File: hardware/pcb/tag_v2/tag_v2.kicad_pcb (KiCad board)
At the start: 2 copper layers, 87.6 x 50.8 mm, 16 parts

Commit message: *: Update after the first PCB assembly.
- Replaced the 200k ohm resistor with 100k ohm on tag_v2, as GPIO pin 32
  reduces the voltage somehow, updated the battery voltage divider
  accordingly in tag.ino

- Fix an issue of tag LED as the tag will not invoke newDevice() even
  though it's added by the Sensor.

- Updated the DRIVE_MODE_MANUAL to be long steady light instead of
  blincking.

- Fixed a short wiring issue on the sensor.
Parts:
- R5: value 220KΩ -> 100KΩ
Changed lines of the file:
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@@
 			)
 		)
-		(property "Value" "220KΩ"
+		(property "Value" "100KΩ"
 			(at 3.81 0 90)
 			(unlocked yes)

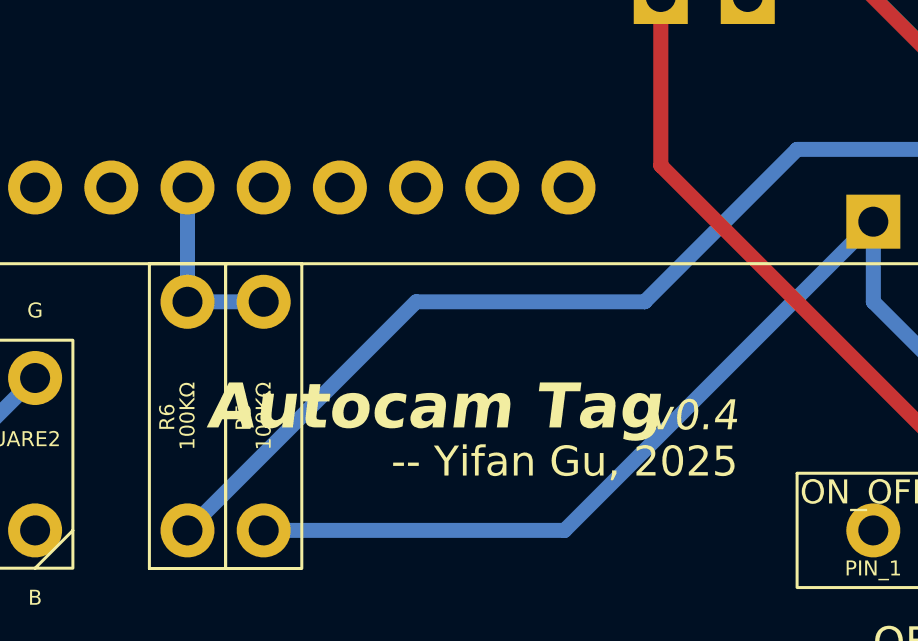
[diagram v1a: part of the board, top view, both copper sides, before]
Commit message: remote: Update PCB for remote.
Fix the issue that GPIO 35 does not have internal PULLUP resistor.
So switch the pin with the gimbal thumbstick input Y, instead of the
drive mode button.

Update sensor and tag pcb as well to reflect the changes.
- tag: Use pin 39 for battery measurement and revert the resistor value
  change that's done in the previous commit.
- sensor: Fix a wiring issue.
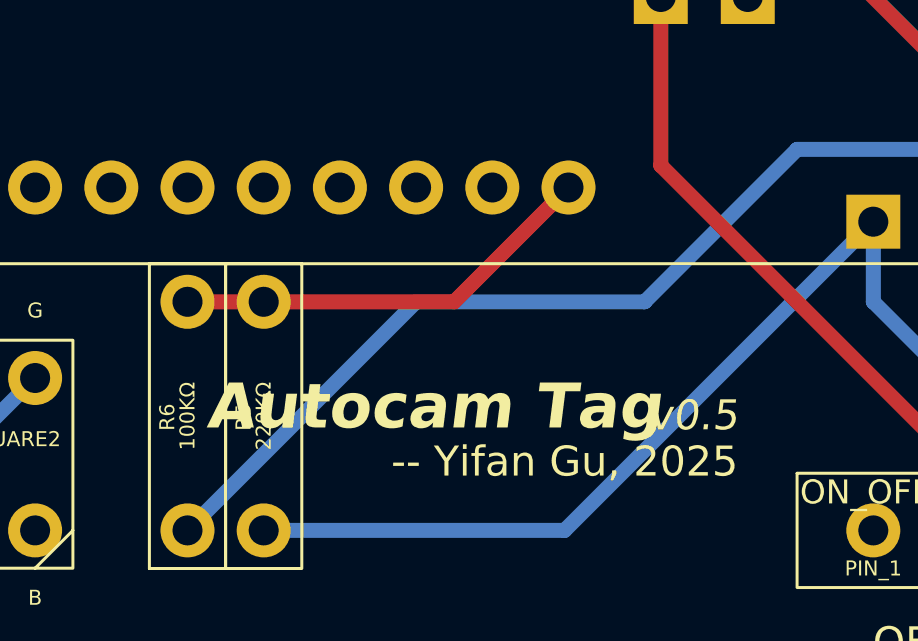
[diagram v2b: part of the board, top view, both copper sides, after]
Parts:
- R5: value 100KΩ -> 220KΩ
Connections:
- ESP32_UWB1 pad 15: Net-(ESP32_UWB1-IO32) -> unconnected-(ESP32_UWB1-IO32-Pad15)
- ESP32_UWB1 pad 20: unconnected-(ESP32_UWB1-IO39-Pad20) -> Net-(ESP32_UWB1-IO39)
- R5 pad 2: Net-(ESP32_UWB1-IO32) -> Net-(ESP32_UWB1-IO39)
- R6 pad 2: Net-(ESP32_UWB1-IO32) -> Net-(ESP32_UWB1-IO39)
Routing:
- net Net-(ESP32_UWB1-IO39): track 0.00 -> 14.3 mm
- net Net-(ESP32_UWB1-IO32): track 6.35 -> 0.00 mm
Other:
- board text added: "v0.5"
- board text removed: "v0.4"
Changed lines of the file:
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@@
 	(title_block
 		(title "Autocam Tag")
-		(date "2025-03-18")
-		(rev "v0.4")
+		(date "2025-03-27")
+		(rev "v0.5")
 	)
 	(layers
@@
 	(net 36 "Net-(ESP32_UWB1-IO2)")
 	(net 37 "unconnected-(ESP32_UWB1-IO15-Pad9)")
-	(net 38 "unconnected-(ESP32_UWB1-IO39-Pad20)")
-	(net 39 "Net-(ESP32_UWB1-IO32)")
+	(net 38 "Net-(ESP32_UWB1-IO39)")
+	(net 39 "unconnected-(ESP32_UWB1-IO32-Pad15)")
 	(net 40 "Net-(RGB_LED_SQUARE1-R)")
 	(net 41 "Net-(RGB_LED_SQUARE1-G)")
@@
 			(layers "*.Cu" "*.Mask")
 			(remove_unused_layers no)
-			(net 39 "Net-(ESP32_UWB1-IO32)")
+			(net 39 "unconnected-(ESP32_UWB1-IO32-Pad15)")
 			(pinfunction "IO32")
 			(pintype "bidirectional")
@@
 			(layers "*.Cu" "*.Mask")
 			(remove_unused_layers no)
-			(net 38 "unconnected-(ESP32_UWB1-IO39-Pad20)")
+			(net 38 "Net-(ESP32_UWB1-IO39)")
 			(pinfunction "IO39")
 			(pintype "bidirectional")
@@
 			(layers "*.Cu" "*.Mask")
 			(remove_unused_layers no)
-			(net 39 "Net-(ESP32_UWB1-IO32)")
+			(net 38 "Net-(ESP32_UWB1-IO39)")
 			(pintype "passive")
 		)
@@
 			)
 		)
-		(property "Value" "100KΩ"
+		(property "Value" "220KΩ"
 			(at 3.81 0 90)
 			(unlocked yes)
@@
 			(layers "*.Cu" "*.Mask")
 			(remove_unused_layers no)
-			(net 39 "Net-(ESP32_UWB1-IO32)")
+			(net 38 "Net-(ESP32_UWB1-IO39)")
 			(pintype "passive")
 		)
@@
 		(layer "Edge.Cuts")
 	)
-	(gr_text "v0.4"
+	(gr_text "v0.5"
 		(at 169.485555 119.942652 0)
 		(layer "F.SilkS")
@@
 			(justify right bottom)
 		)
-		(render_cache "v0.4" 0
+		(render_cache "v0.5" 0
 			(polygon
 				(pts
@@
 			(polygon
 				(pts
-					(xy 168.919339 119.273724) (xy 168.952434 118.896308) (xy 169.039018 118.994921) (xy 169.017341 119.249483)
-					(xy 168.952434 119.309384)
+					(xy 169.469191 118.881654) (xy 169.367341 118.975443) (xy 169.058069 118.975443) (xy 168.971546 118.881654)
 				)
 			)
 			(polygon
 				(pts
-					(xy 169.443728 119.381924) (xy 169.410634 119.757997) (xy 169.325332 119.659323) (xy 169.347008 119.404822)
-					(xy 169.411916 119.345043)
+					(xy 169.391522 119.772652) (xy 168.893877 119.772652) (xy 168.996947 119.678862) (xy 169.30622 119.678862)
+				)
+			)
+			(polygon
+				(pts
+					(xy 168.919339 119.273724) (xy 168.952434 118.899544) (xy 169.039018 118.994982) (xy 169.017341 119.249483)
+					(xy 168.952434 119.309384)
 				)
 			)
 			(polygon
 				(pts
-					(xy 169.360991 119.249483) (xy 169.382607 118.995104) (xy 169.485738 118.896308) (xy 169.452643 119.273724)
-					(xy 169.415702 119.309384)
+					(xy 169.443728 119.381924) (xy 169.410634 119.753112) (xy 169.325332 119.659262) (xy 169.347008 119.404883)
+					(xy 169.411916 119.345043)
 				)
 			)
@@
 	(segment
 		(start 153.67 115.57)
-		(end 151.13 115.57)
+		(end 160.02 115.57)
 		(width 0.5)
-		(layer "B.Cu")
-		(net 39)
+		(layer "F.Cu")
+		(net 38)
 	)
 	(segment
-		(start 151.13 111.76)
+		(start 160.02 115.57)
+		(end 163.83 111.76)
+		(width 0.5)
+		(layer "F.Cu")
+		(net 38)
+	)
+	(segment
+		(start 153.67 115.57)
 		(end 151.13 115.57)
 		(width 0.5)
-		(layer "B.Cu")
-		(net 39)
+		(layer "F.Cu")
+		(net 38)
 	)
 	(segment

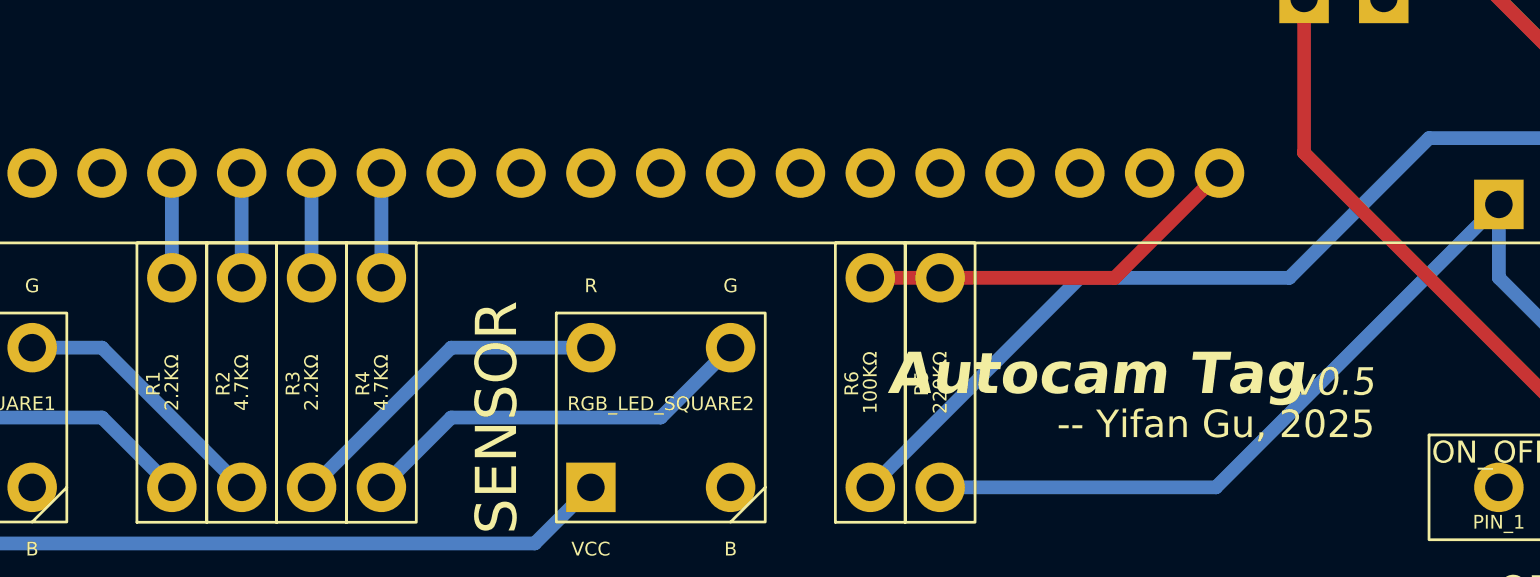
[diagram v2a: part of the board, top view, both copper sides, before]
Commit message: sensor,tag: Update PCB wiring to avoid bootstrap pins.
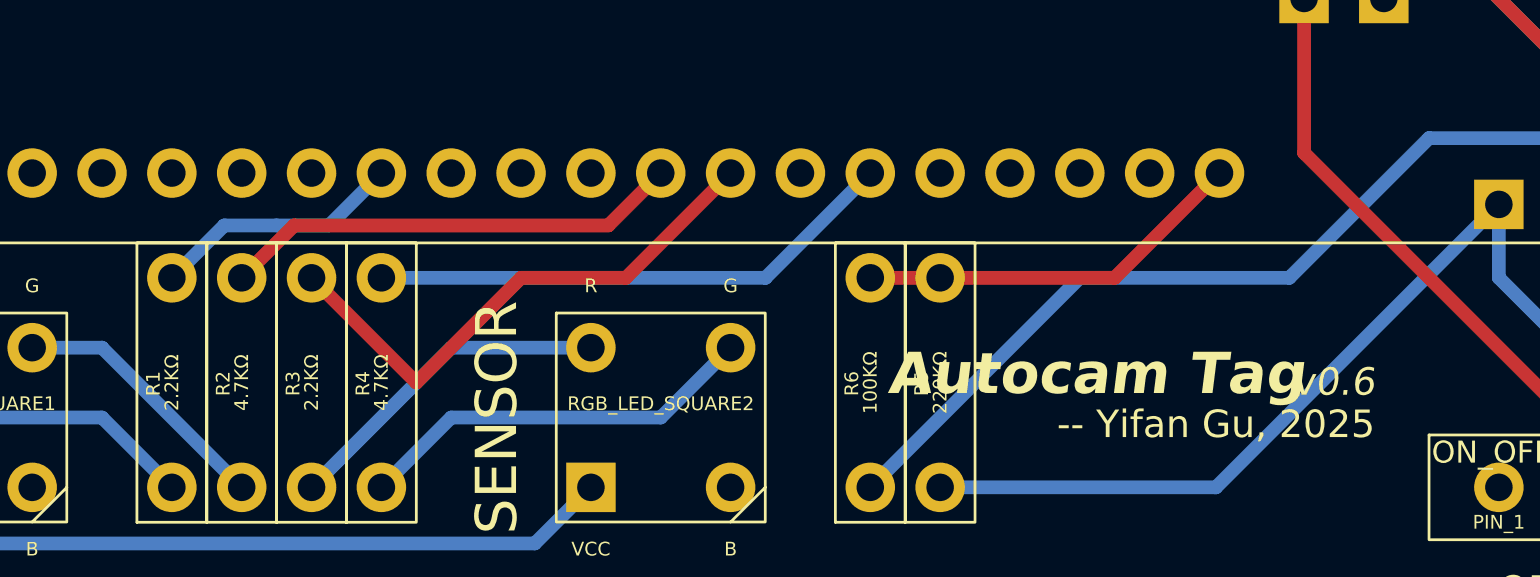
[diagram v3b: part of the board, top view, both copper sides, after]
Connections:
- ESP32_UWB1 pad 12: unconnected-(ESP32_UWB1-IO25-Pad12) -> Net-(ESP32_UWB1-IO25)
- ESP32_UWB1 pad 13: unconnected-(ESP32_UWB1-IO26-Pad13) -> Net-(ESP32_UWB1-IO26)
- ESP32_UWB1 pad 15: unconnected-(ESP32_UWB1-IO32-Pad15) -> Net-(ESP32_UWB1-IO32)
- ESP32_UWB1 pad 5: Net-(ESP32_UWB1-IO2) -> unconnected-(ESP32_UWB1-IO2-Pad5)
- ESP32_UWB1 pad 6: Net-(ESP32_UWB1-IO12) -> unconnected-(ESP32_UWB1-IO12-Pad6)
- ESP32_UWB1 pad 7: Net-(ESP32_UWB1-IO13) -> unconnected-(ESP32_UWB1-IO13-Pad7)
- R1 pad 2: Net-(ESP32_UWB1-IO2) -> Net-(ESP32_UWB1-IO14)
- R2 pad 2: Net-(ESP32_UWB1-IO12) -> Net-(ESP32_UWB1-IO25)
- R3 pad 2: Net-(ESP32_UWB1-IO13) -> Net-(ESP32_UWB1-IO26)
- R4 pad 2: Net-(ESP32_UWB1-IO14) -> Net-(ESP32_UWB1-IO32)
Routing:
- net Net-(ESP32_UWB1-IO26): track 0.00 -> 20.0 mm
- net Net-(ESP32_UWB1-IO32): track 0.00 -> 19.4 mm
- net Net-(ESP32_UWB1-IO25): track 0.00 -> 16.8 mm
- net Net-(ESP32_UWB1-IO14): track 3.81 -> 9.20 mm
- net Net-(ESP32_UWB1-IO2): track 3.81 -> 0.00 mm
- net Net-(ESP32_UWB1-IO13): track 3.81 -> 0.00 mm
- net Net-(ESP32_UWB1-IO12): track 3.81 -> 0.00 mm
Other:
- board text added: "v0.6"
- board text removed: "v0.5"
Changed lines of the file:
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@@
 		(title "Autocam Tag")
 		(date "2025-03-27")
-		(rev "v0.5")
+		(rev "v0.6")
 	)
 	(layers
@@
 	)
 	(net 0 "")
-	(net 1 "unconnected-(ESP32_UWB1-IO25-Pad12)")
+	(net 1 "Net-(ESP32_UWB1-IO25)")
 	(net 2 "unconnected-(ESP32_UWB1-IO27-Pad14)")
 	(net 3 "unconnected-(ESP32_UWB1-IO22-Pad31)")
@@
 	(net 9 "unconnected-(ESP32_UWB1-IO4-Pad26)")
 	(net 10 "unconnected-(ESP32_UWB1-IO19-Pad11)")
-	(net 11 "Net-(ESP32_UWB1-IO12)")
+	(net 11 "unconnected-(ESP32_UWB1-IO13-Pad7)")
 	(net 12 "Net-(ESP32_UWB1-IO14)")
 	(net 13 "unconnected-(ESP32_UWB1-IO17-Pad29)")
-	(net 14 "Net-(ESP32_UWB1-IO13)")
-	(net 15 "unconnected-(ESP32_UWB1-IO26-Pad13)")
+	(net 14 "unconnected-(ESP32_UWB1-IO15-Pad9)")
+	(net 15 "Net-(ESP32_UWB1-IO26)")
 	(net 16 "unconnected-(ESP32_UWB1-IO1-Pad24)")
 	(net 17 "unconnected-(ESP32_UWB1-IO33-Pad16)")
@@
 	(net 34 "Net-(5V_DC_DC_Converter1-OUT)")
 	(net 35 "Net-(5V_DC_DC_Converter1-IN)")
-	(net 36 "Net-(ESP32_UWB1-IO2)")
-	(net 37 "unconnected-(ESP32_UWB1-IO15-Pad9)")
+	(net 36 "unconnected-(ESP32_UWB1-IO2-Pad5)")
+	(net 37 "Net-(ESP32_UWB1-IO32)")
 	(net 38 "Net-(ESP32_UWB1-IO39)")
-	(net 39 "unconnected-(ESP32_UWB1-IO32-Pad15)")
+	(net 39 "unconnected-(ESP32_UWB1-IO12-Pad6)")
 	(net 40 "Net-(RGB_LED_SQUARE1-R)")
 	(net 41 "Net-(RGB_LED_SQUARE1-G)")
@@
 			(layers "*.Cu" "*.Mask")
 			(remove_unused_layers no)
-			(net 36 "Net-(ESP32_UWB1-IO2)")
+			(net 36 "unconnected-(ESP32_UWB1-IO2-Pad5)")
 			(pinfunction "IO2")
 			(pintype "bidirectional")
@@
 			(layers "*.Cu" "*.Mask")
 			(remove_unused_layers no)
-			(net 11 "Net-(ESP32_UWB1-IO12)")
+			(net 39 "unconnected-(ESP32_UWB1-IO12-Pad6)")
 			(pinfunction "IO12")
 			(pintype "bidirectional")
@@
 			(layers "*.Cu" "*.Mask")
 			(remove_unused_layers no)
-			(net 14 "Net-(ESP32_UWB1-IO13)")
+			(net 11 "unconnected-(ESP32_UWB1-IO13-Pad7)")
 			(pinfunction "IO13")
 			(pintype "bidirectional")
@@
 			(layers "*.Cu" "*.Mask")
 			(remove_unused_layers no)
-			(net 37 "unconnected-(ESP32_UWB1-IO15-Pad9)")
+			(net 14 "unconnected-(ESP32_UWB1-IO15-Pad9)")
 			(pinfunction "IO15")
 			(pintype "bidirectional")
@@
 			(layers "*.Cu" "*.Mask")
 			(remove_unused_layers no)
-			(net 1 "unconnected-(ESP32_UWB1-IO25-Pad12)")
+			(net 1 "Net-(ESP32_UWB1-IO25)")
 			(pinfunction "IO25")
 			(pintype "bidirectional")
@@
 			(layers "*.Cu" "*.Mask")
 			(remove_unused_layers no)
-			(net 15 "unconnected-(ESP32_UWB1-IO26-Pad13)")
+			(net 15 "Net-(ESP32_UWB1-IO26)")
 			(pinfunction "IO26")
 			(pintype "bidirectional")
@@
 			(layers "*.Cu" "*.Mask")
 			(remove_unused_layers no)
-			(net 39 "unconnected-(ESP32_UWB1-IO32-Pad15)")
+			(net 37 "Net-(ESP32_UWB1-IO32)")
 			(pinfunction "IO32")
 			(pintype "bidirectional")
@@
 			(layers "*.Cu" "*.Mask")
 			(remove_unused_layers no)
-			(net 36 "Net-(ESP32_UWB1-IO2)")
+			(net 12 "Net-(ESP32_UWB1-IO14)")
 			(pintype "passive")
 		)
@@
 			(layers "*.Cu" "*.Mask")
 			(remove_unused_layers no)
-			(net 11 "Net-(ESP32_UWB1-IO12)")
+			(net 1 "Net-(ESP32_UWB1-IO25)")
 			(pintype "passive")
 		)
@@
 			(layers "*.Cu" "*.Mask")
 			(remove_unused_layers no)
-			(net 12 "Net-(ESP32_UWB1-IO14)")
+			(net 37 "Net-(ESP32_UWB1-IO32)")
 			(pintype "passive")
 		)
@@
 			(layers "*.Cu" "*.Mask")
 			(remove_unused_layers no)
-			(net 14 "Net-(ESP32_UWB1-IO13)")
+			(net 15 "Net-(ESP32_UWB1-IO26)")
 			(pintype "passive")
 		)
@@
 		(layer "Edge.Cuts")
 	)
-	(gr_text "v0.5"
+	(gr_text "v0.6"
 		(at 169.485555 119.942652 0)
 		(layer "F.SilkS")
@@
 			(justify right bottom)
 		)
-		(render_cache "v0.5" 0
+		(render_cache "v0.6" 0
 			(polygon
 				(pts
@@
 			(polygon
 				(pts
-					(xy 169.391522 119.772652) (xy 168.893877 119.772652) (xy 168.996947 119.678862) (xy 169.30622 119.678862)
+					(xy 169.391522 119.772652) (xy 168.893877 119.772652) (xy 168.997008 119.678862) (xy 169.306281 119.678862)
+				)
+			)
+			(polygon
+				(pts
+					(xy 169.003359 119.404761) (xy 168.981743 119.659262) (xy 168.877329 119.753112) (xy 168.910424 119.381863)
+					(xy 168.948587 119.345043)
 				)
 			)
@@
 			(polygon
 				(pts
-					(xy 169.443728 119.381924) (xy 169.410634 119.753112) (xy 169.325332 119.659262) (xy 169.347008 119.404883)
+					(xy 169.443728 119.381924) (xy 169.410634 119.754822) (xy 169.325332 119.659323) (xy 169.347008 119.404883)
 					(xy 169.411916 119.345043)
 				)
@@
 				(pts
 					(xy 169.352076 119.280258) (xy 169.396651 119.327153) (xy 169.343161 119.374047) (xy 169.010991 119.374047)
-					(xy 168.968981 119.327153) (xy 169.019906 119.280258)
+					(xy 168.968981 119.327214) (xy 169.019906 119.280441)
 				)
 			)
@@
 	)
 	(segment
+		(start 141.605 113.665)
+		(end 130.175 113.665)
+		(width 0.5)
+		(layer "F.Cu")
+		(net 1)
+	)
+	(segment
+		(start 143.51 111.76)
+		(end 141.605 113.665)
+		(width 0.5)
+		(layer "F.Cu")
+		(net 1)
+	)
+	(segment
+		(start 128.27 115.57)
+		(end 130.175 113.665)
+		(width 0.5)
+		(layer "F.Cu")
+		(net 1)
+	)
+	(segment
 		(start 117.61 125.23)
 		(end 138.93 125.23)
@@
 	)
 	(segment
-		(start 128.27 111.76)
-		(end 128.27 115.57)
+		(start 129.54 113.665)
+		(end 131.445 113.665)
 		(width 0.5)
 		(layer "B.Cu")
-		(net 11)
+		(net 12)
 	)
 	(segment
-		(start 133.35 111.76)
-		(end 133.35 115.57)
+		(start 131.445 113.665)
+		(end 133.35 111.76)
 		(width 0.5)
 		(layer "B.Cu")
@@
 	)
 	(segment
-		(start 130.81 115.57)
-		(end 130.81 111.76)
+		(start 125.73 115.57)
+		(end 127.635 113.665)
 		(width 0.5)
 		(layer "B.Cu")
-		(net 14)
+		(net 12)
+	)
+	(segment
+		(start 127.635 113.665)
+		(end 129.54 113.665)
+		(width 0.5)
+		(layer "B.Cu")
+		(net 12)
+	)
+	(segment
+		(start 146.05 111.76)
+		(end 142.24 115.57)
+		(width 0.5)
+		(layer "F.Cu")
+		(net 15)
+	)
+	(segment
+		(start 142.24 115.57)
+		(end 138.43 115.57)
+		(width 0.5)
+		(layer "F.Cu")
+		(net 15)
+	)
+	(segment
+		(start 138.43 115.57)
+		(end 134.62 119.38)
+		(width 0.5)
+		(layer "F.Cu")
+		(net 15)
+	)
+	(segment
+		(start 134.62 119.38)
+		(end 130.81 115.57)
+		(width 0.5)
+		(layer "F.Cu")
+		(net 15)
 	)
 	(segment
@@
 	)
 	(segment
-		(start 125.73 115.57)
-		(end 125.73 111.76)
+		(start 147.32 115.57)
+		(end 151.13 111.76)
+		(width 0.5)
+		(layer "B.Cu")
+		(net 37)
+	)
+	(segment
+		(start 133.35 115.57)
+		(end 147.32 115.57)
 		(width 0.5)
 		(layer "B.Cu")
-		(net 36)
+		(net 37)
 	)
 	(segment
